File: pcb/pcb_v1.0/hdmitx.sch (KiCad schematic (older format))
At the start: 32 parts, among them J4 HDMI_CONN, U15 TLV70018, U16 TLV70018, U3 IT6613

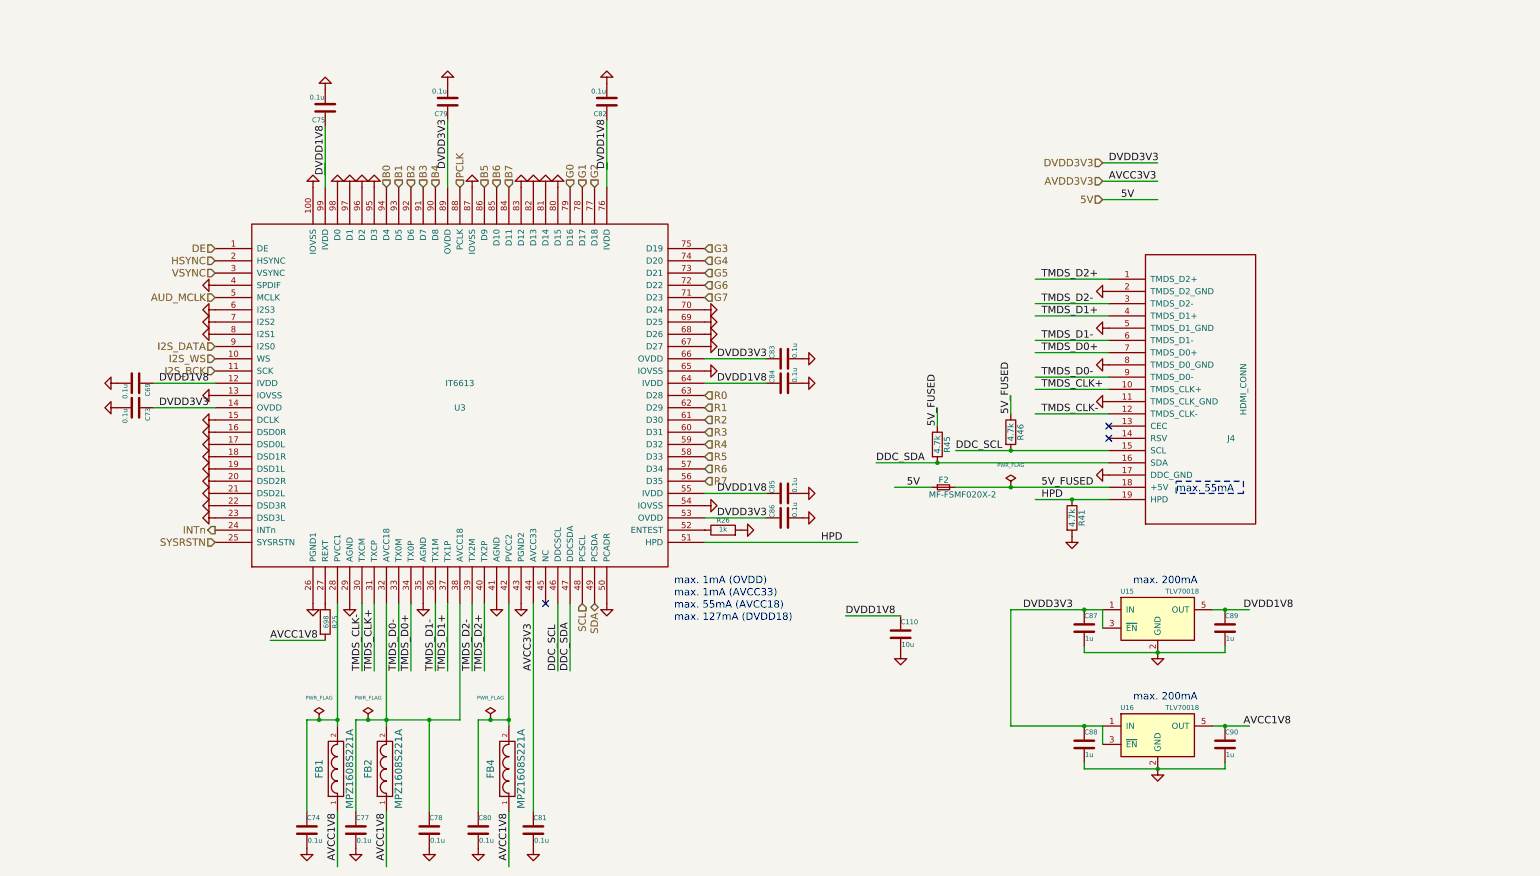
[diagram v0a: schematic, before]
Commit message: This is a combination of 10 commits.
Moved ICs to top, made to fit ontop of CPS2 DIPs

Added ADV7513

update lib path

Finished power section of ADV7531

initial layout of ADV7513

Added Si5351C

Reordered inputs, improved clock layout

Final changes before pull req

Removing auto-generated files

Removing remaining auto-generated files
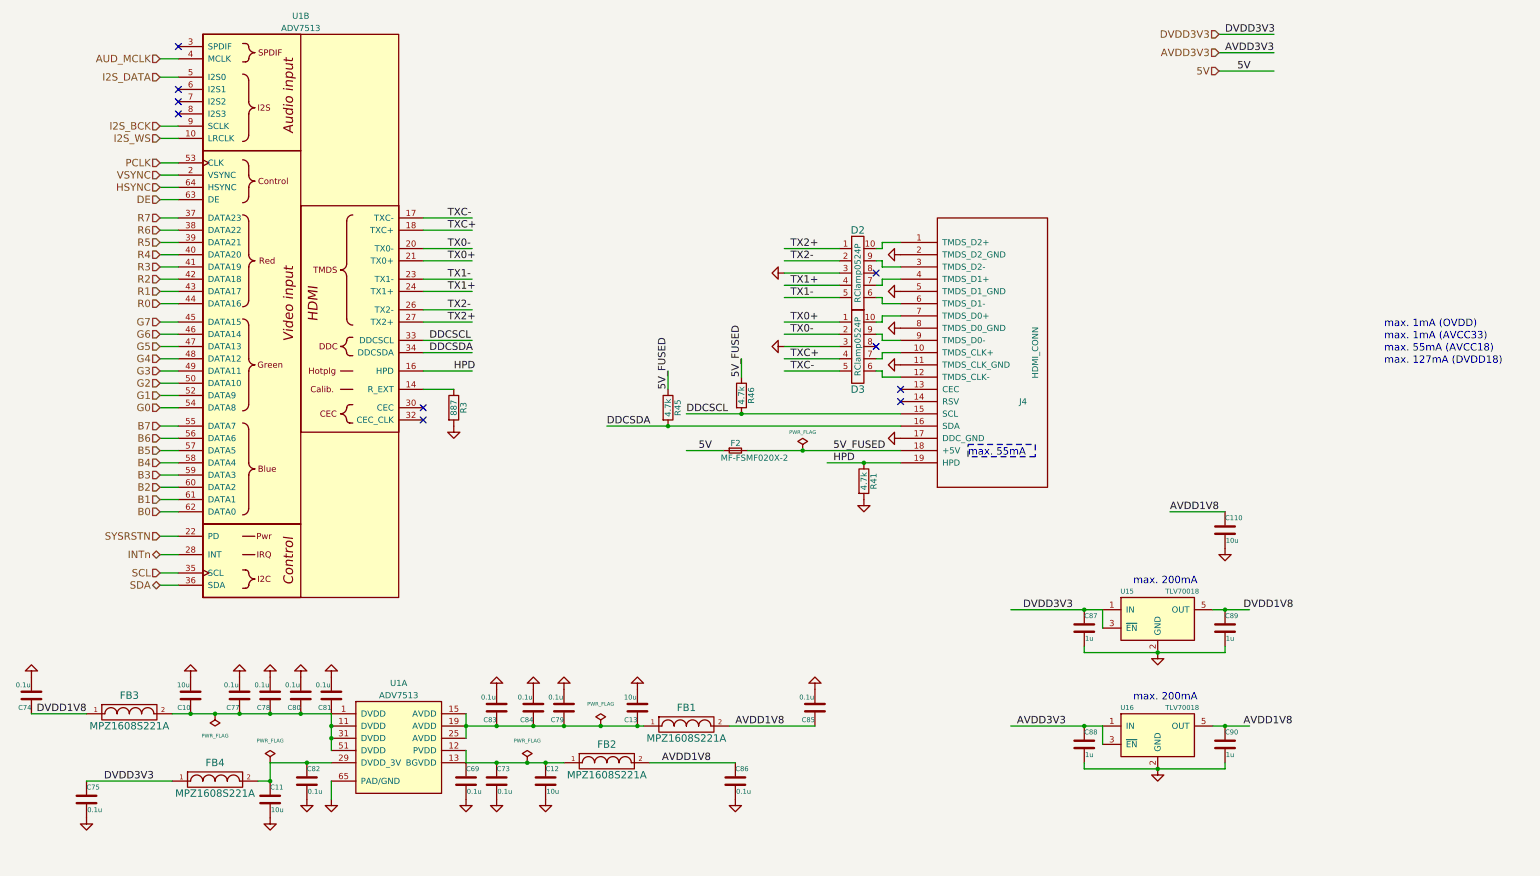
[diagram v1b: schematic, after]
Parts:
- removed R25: 698, custom_components:SM0603_Resistor_libcms, symbol R
- removed R26: 1k, custom_components:SM0603_Resistor_libcms, symbol R
- removed U3: IT6613, custom_components:TQFP-100_custom, symbol IT6613
- added C10, C11, C12, C13: 10u, custom_components:SM0603_Capa_libcms, symbol C
- added D2, D3: RClamp0524P, Custom_OSSC:SLP2510P8, symbol RClamp0524P
- added FB3: MPZ1608S221A, custom_components:SM0603_Resistor_libcms, symbol FILTER
- added R3: 887, custom_components:SM0603_Resistor_libcms, symbol R
- added U1: ADV7513, Housings_QFP:LQFP-64-1EP_10x10mm_Pitch0.5mm, symbol ADV7513
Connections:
- net labels added: AVDD1V8, DDCSCL, DDCSDA, TX0+, TX0-, TX1+, TX1-, TX2+, TX2-, TXC+, TXC-
- net labels removed: AVCC1V8, AVCC3V3, DDC_SCL, DDC_SDA, TMDS_CLK+, TMDS_CLK-, TMDS_D0+, TMDS_D0-, TMDS_D1+, TMDS_D1-, TMDS_D2+, TMDS_D2-
- wire segments 70 -> 119
- no-connect marks 3 -> 10
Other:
- moved on the sheet: C110, C69, C73, C74, C75, C77, C78, C79, C80, C81, C82, C83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

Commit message: fix schematic and library linkage issues
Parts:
- D2, D3: footprint Custom_OSSC:SLP2510P8 -> custom_components:SLP2510P8
- F2: symbol F_Small -> Fuse_Small
- FB1, FB2, FB3, FB4: symbol FILTER -> Ferrite_Bead
- U15, U16: symbol TLV71209DBV -> TLV70018_SOT23-5
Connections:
- wire segments 119 -> 115
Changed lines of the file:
@@
 LIBS:valves
 LIBS:custom_components
-LIBS:74lvc
-LIBS:altera
-LIBS:analog_devices
-LIBS:barrel_jack
-LIBS:battery
-LIBS:beaglebone_black
-LIBS:ck
-LIBS:conn_power
-LIBS:conn_rf
-LIBS:conn_rj
-LIBS:crystal
-LIBS:ddr2_sdram_sodimm
-LIBS:diode
-LIBS:epcos
-LIBS:epcos_dcc6c
-LIBS:fbead
-LIBS:fiducial
-LIBS:freescale_mcu
-LIBS:hackrf_expansion
-LIBS:hdmi
-LIBS:header
-LIBS:hirose
-LIBS:hole
-LIBS:io_expander
-LIBS:lcd_kingtech
-LIBS:ltc
-LIBS:microphone
-LIBS:minicircuits
-LIBS:molex
-LIBS:mosfet
-LIBS:newhaven
-LIBS:noritake
-LIBS:nxp_micro
-LIBS:on_cat24c256
-LIBS:on_semi
-LIBS:osc
-LIBS:passive
-LIBS:regulator
-LIBS:rf_antenna
-LIBS:rf_lna
-LIBS:r_sense
-LIBS:samtec
-LIBS:sd
-LIBS:sharebrained
-LIBS:silabs
-LIBS:supply
-LIBS:switch
-LIBS:terminal_block
-LIBS:ti
-LIBS:ti_cc
-LIBS:tp
-LIBS:trs_jack
-LIBS:usb3_esd_son50-10
-LIBS:usb3_micro_ab
-LIBS:wolfson
-LIBS:ossc_board-cache
+LIBS:HDMI
 LIBS:cps2_digiav-cache
 EELAYER 25 0
@@
 Title "CPS2_digiAV"
 Date "2016-09-24"
-Rev "1.0"
+Rev "2.0"
 Comp ""
 Comment1 ""
@@
 $EndComp
 $Comp
-L FILTER FB1
+L Ferrite_Bead FB1
 U 1 1 5501ED08
 P 6100 6500
-F 0 "FB1" H 6100 6650 60  0000 C CNN
-F 1 "MPZ1608S221A" H 6100 6400 60  0000 C CNN
+F 0 "FB1" V 5950 6550 60  0000 C CNN
+F 1 "MPZ1608S221A" V 6250 6500 60  0000 C CNN
 F 2 "custom_components:SM0603_Resistor_libcms" H 6100 6500 60  0001 C CNN
 F 3 "~" H 6100 6500 60  0000 C CNN
 	1    6100 6500
-	1    0    0    -1
+	0    1    1    0
 $EndComp
 $Comp
@@
 $EndComp
 $Comp
-L FILTER FB2
+L Ferrite_Bead FB2
 U 1 1 5501F495
 P 5450 6800
-F 0 "FB2" H 5450 6950 60  0000 C CNN
-F 1 "MPZ1608S221A" H 5450 6700 60  0000 C CNN
+F 0 "FB2" V 5300 6900 60  0000 C CNN
+F 1 "MPZ1608S221A" V 5600 6850 60  0000 C CNN
 F 2 "custom_components:SM0603_Resistor_libcms" H 5450 6800 60  0001 C CNN
 F 3 "~" H 5450 6800 60  0000 C CNN
 	1    5450 6800
-	1    0    0    -1
+	0    1    1    0
 $EndComp
 $Comp
@@
 DVDD3V3
 $Comp
-L TLV71209DBV U15
+L TLV70018_SOT23-5 U15
 U 1 1 5502F816
 P 9950 5600
@@
 DVDD1V8
 $Comp
-L TLV71209DBV U16
+L TLV70018_SOT23-5 U16
 U 1 1 5502F844
 P 9950 6550
@@
 $EndComp
 $Comp
-L FILTER FB4
+L Ferrite_Bead FB4
 U 1 1 5501F45A
 P 2250 6950
-F 0 "FB4" H 2250 7100 60  0000 C CNN
-F 1 "MPZ1608S221A" H 2250 6850 60  0000 C CNN
+F 0 "FB4" V 2100 6950 60  0000 C CNN
+F 1 "MPZ1608S221A" V 2450 6900 60  0000 C CNN
 F 2 "custom_components:SM0603_Resistor_libcms" H 2250 6950 60  0001 C CNN
 F 3 "~" H 2250 6950 60  0000 C CNN
 	1    2250 6950
-	1    0    0    -1
+	0    1    1    0
 $EndComp
 $Comp
@@
 DDCSDA
 $Comp
-L F_Small F2
+L Fuse_Small F2
 U 1 1 5686BBED
 P 6500 4250
@@
 HPD
 $Comp
-L FILTER FB3
+L Ferrite_Bead FB3
 U 1 1 5A3CCA28
 P 1550 6400
-F 0 "FB3" H 1550 6550 60  0000 C CNN
-F 1 "MPZ1608S221A" H 1550 6300 60  0000 C CNN
+F 0 "FB3" V 1350 6400 60  0000 C CNN
+F 1 "MPZ1608S221A" V 1700 6350 60  0000 C CNN
 F 2 "custom_components:SM0603_Resistor_libcms" H 1550 6400 60  0001 C CNN
 F 3 "~" H 1550 6400 60  0000 C CNN
 	1    1550 6400
-	1    0    0    -1
+	0    1    1    0
 $EndComp
 $Comp
@@
 F 0 "D2" H 7500 3150 60  0000 C CNN
 F 1 "RClamp0524P" V 7500 2800 50  0000 C CNN
-F 2 "Custom_OSSC:SLP2510P8" H 7550 2850 60  0001 C CNN
+F 2 "custom_components:SLP2510P8" H 7550 2850 60  0001 C CNN
 F 3 "" H 7550 2850 60  0001 C CNN
 	1    7500 2800
@@
 F 0 "D3" H 7500 3050 60  0000 C CNN
 F 1 "RClamp0524P" V 7500 3400 50  0000 C CNN
-F 2 "Custom_OSSC:SLP2510P8" H 7550 3450 60  0001 C CNN
+F 2 "custom_components:SLP2510P8" H 7550 3450 60  0001 C CNN
 F 3 "" H 7550 3450 60  0001 C CNN
 	1    7500 3400
@@
 $EndComp
 Wire Wire Line
-	6900 2600 7350 2600
-Wire Wire Line
-	6900 2700 7350 2700
-Wire Wire Line
-	6900 2900 7350 2900
-Wire Wire Line
-	6900 3000 7350 3000
-Wire Wire Line
-	6900 3200 7350 3200
-Wire Wire Line
-	6900 3300 7350 3300
-Wire Wire Line
-	6900 3500 7350 3500
-Wire Wire Line
-	6900 3600 7350 3600
+	6900 2600 7700 2600
+Wire Wire Line
+	6900 2700 7700 2700
+Wire Wire Line
+	6900 2900 7700 2900
+Wire Wire Line
+	6900 3000 7750 3000
+Wire Wire Line
+	6900 3200 7700 3200
+Wire Wire Line
+	6900 3300 7700 3300
+Wire Wire Line
+	6900 3500 7700 3500
+Wire Wire Line
+	6900 3600 7700 3600
 Wire Wire Line
 	10900 1000 10450 1000
@@
 Wire Wire Line
 	10400 5550 10700 5550
-Wire Wire Line
-	9500 5550 9500 5700
 Connection ~ 9350 6500
 Wire Wire Line
-	8750 6500 9500 6500
+	8750 6500 9650 6500
 Wire Wire Line
 	10400 6500 10700 6500
-Wire Wire Line
-	9500 6500 9500 6650
 Wire Notes Line
 	8400 4200 8950 4200
@@
 	8400 4300 8400 4200
 Wire Wire Line
-	8750 5550 9500 5550
+	8750 5550 9650 5550
 Wire Wire Line
 	10050 4750 10500 4750
@@
 Connection ~ 2700 6950
 Wire Wire Line
-	750  6400 1200 6400
-Wire Wire Line
-	1200 6950 1900 6950
-Wire Wire Line
-	2600 6950 2700 6950
+	750  6400 1400 6400
+Wire Wire Line
+	1200 6950 2100 6950
+Wire Wire Line
+	2400 6950 2700 6950
 Connection ~ 3000 6800
 Wire Wire Line
@@
 Connection ~ 4550 6500
 Wire Wire Line
-	6450 6500 7150 6500
+	6250 6500 7150 6500
 Connection ~ 2050 6400
 Connection ~ 2450 6400
@@
 Connection ~ 2950 6400
 Wire Wire Line
-	1900 6400 3200 6400
+	1700 6400 3200 6400
 Connection ~ 2250 6400
 Wire Wire Line
@@
 	2700 6800 3200 6800
 Wire Wire Line
-	4300 6500 5750 6500
+	4300 6500 5950 6500
 Connection ~ 5400 6500
 Wire Wire Line
-	4300 6800 5100 6800
+	4300 6800 5300 6800
 Connection ~ 4800 6800
 Wire Wire Line
-	6500 6800 5800 6800
+	5600 6800 6500 6800
 Wire Wire Line
 	3950 3750 4200 3750
@@
 	6900 3400 7350 3400
 Wire Wire Line
-	7650 2600 7700 2600
-Wire Wire Line
 	7700 2600 7700 2550
 Wire Wire Line
 	7700 2550 7850 2550
 Wire Wire Line
-	7650 2700 7700 2700
-Wire Wire Line
 	7700 2700 7700 2750
 Wire Wire Line
 	7700 2750 7850 2750
 Wire Wire Line
-	7650 2900 7700 2900
-Wire Wire Line
 	7700 2900 7700 2850
 Wire Wire Line
 	7700 2850 7850 2850
 Wire Wire Line
-	7650 3000 7700 3000
-Wire Wire Line
-	7700 3000 7700 3050
-Wire Wire Line
-	7700 3050 7850 3050
-Wire Wire Line
-	7650 3200 7700 3200
-Wire Wire Line
 	7700 3200 7700 3150
 Wire Wire Line
 	7700 3150 7850 3150
 Wire Wire Line
-	7650 3300 7700 3300
-Wire Wire Line
 	7700 3300 7700 3350
 Wire Wire Line
 	7700 3350 7850 3350
 Wire Wire Line
-	7650 3500 7700 3500
-Wire Wire Line
 	7700 3500 7700 3450
 Wire Wire Line
 	7700 3450 7850 3450
-Wire Wire Line
-	7650 3600 7700 3600
 Wire Wire Line
 	7700 3600 7700 3650
@@
 NoConn ~ 7650 2800
 NoConn ~ 7650 3400
+Wire Wire Line
+	9650 5500 9650 5600
+Connection ~ 9650 5550
+Wire Wire Line
+	10250 5500 10400 5500
+Wire Wire Line
+	10400 5500 10400 5550
+Wire Wire Line
+	9650 6450 9650 6550
+Connection ~ 9650 6500
+Wire Wire Line
+	10250 6450 10400 6450
+Wire Wire Line
+	10400 6450 10400 6500
+Wire Wire Line
+	7750 3000 7750 3050
+Wire Wire Line
+	7750 3050 7850 3050
+Connection ~ 7650 2600
+Connection ~ 7350 2600
+Connection ~ 7650 2900
+Connection ~ 7350 2900
+Connection ~ 7350 3000
+Connection ~ 7650 3000
+Connection ~ 7650 3200
+Connection ~ 7350 3200
+Connection ~ 7350 3300
+Connection ~ 7650 3300
+Connection ~ 7650 3500
+Connection ~ 7350 3500
+Connection ~ 7350 3600
+Connection ~ 7650 3600
+Connection ~ 7650 2700
+Connection ~ 7350 2700
 $EndSCHEMATC
